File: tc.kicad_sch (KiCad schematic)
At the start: 6 parts

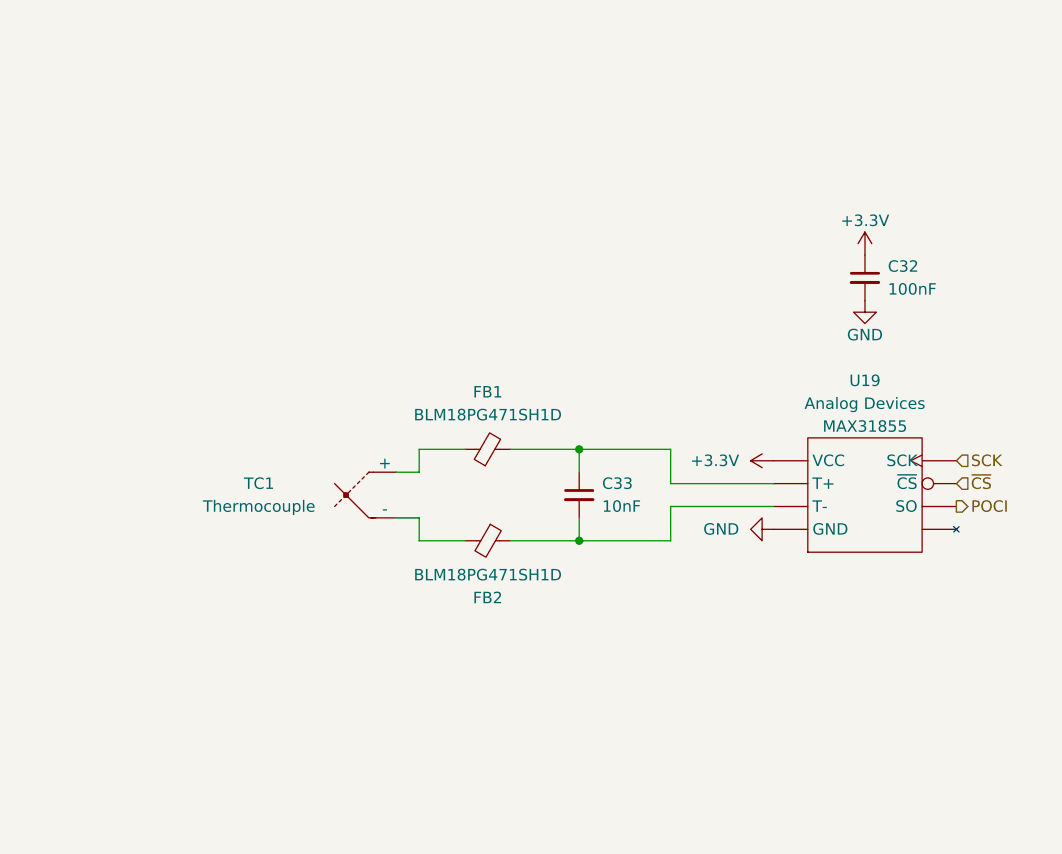
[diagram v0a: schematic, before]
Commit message: Updated schematic. No filtering but besides that finished. Need to fix footprints and start layout.
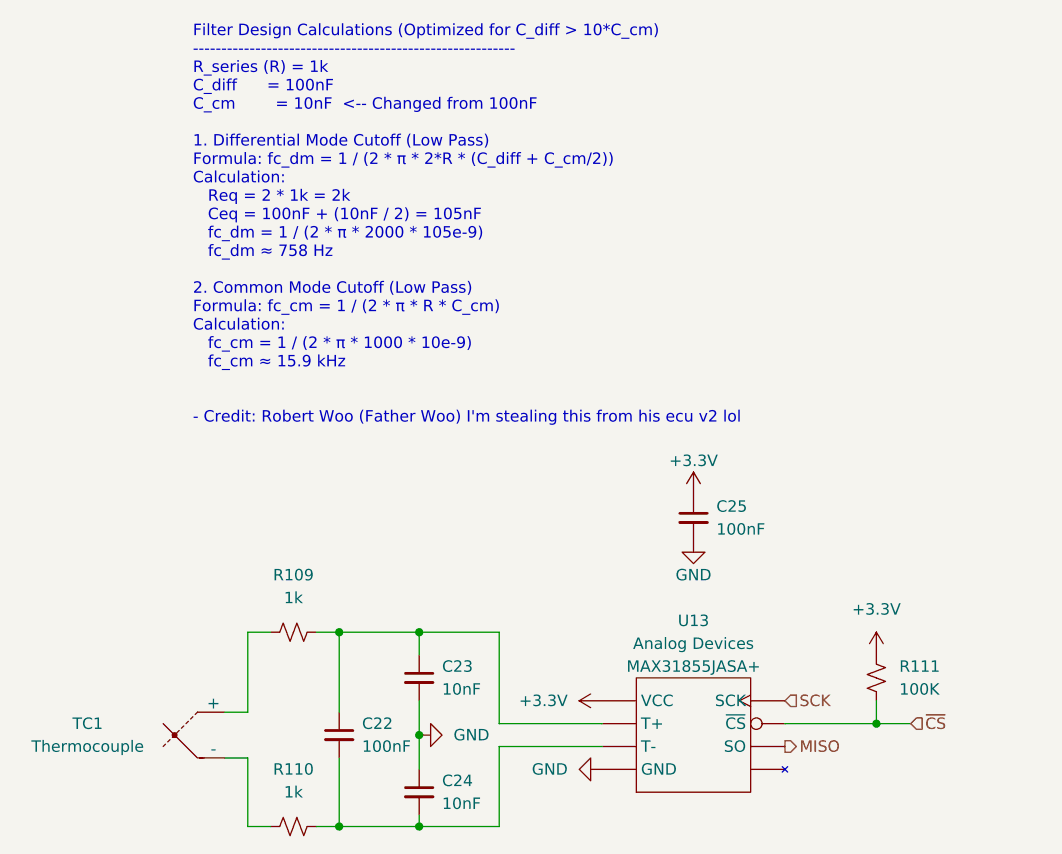
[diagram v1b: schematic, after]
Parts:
- removed C32: 100nF, Capacitor_SMD:C_0402_1005Metric, symbol Device:C_Small
- removed C33: 10nF, Capacitor_SMD:C_0402_1005Metric, symbol Device:C_Small
- removed FB1, FB2: BLM18PG471SH1D, Inductor_SMD:L_0603_1608Metric, symbol Device:FerriteBead_Small
- removed U19: ~, Package_SO:SOIC-8_3.9x4.9mm_P1.27mm, symbol UCIRP-KiCAD-Lib:MAX31855
- added C22, C25: 100nF, Capacitor_SMD:C_0402_1005Metric, symbol Device:C_Small
- added C23, C24: 10nF, Capacitor_SMD:C_0402_1005Metric, symbol Device:C_Small
- added R109, R110: 1k, Resistor_SMD:R_0402_1005Metric, symbol Device:R_Small_US
- added R111: 100K, Resistor_SMD:R_0402_1005Metric, symbol Device:R_Small_US
- added U13: ~, Package_SO:SOIC-8_3.9x4.9mm_P1.27mm, symbol UCIRP-KiCAD-Lib:MAX31855
- TC1: footprint UCIRP-KiCAD-Lib:AM-K-PCB -> 0UCIRP-KiCAD-Lib:AM-K-PCB
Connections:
- net +3.3V: now also C25.1, R111.1, U13.4 (VCC)
- net GND: now also C23.2, C24.1, C25.2, U13.1 (GND)
- net SCK: now also U13.5 (SCK)
- net ~{CS}: now also R111.2, U13.6 (~{CS})
- net at TC1.1 (+): now also R109.1
- net at TC1.2 (-): now also R110.1
- new net: C22.2, C24.2, R110.2, U13.2 (T-)
- new net: C22.1, C23.1, R109.2, U13.3 (T+)
- new net MISO: U13.7 (SO)
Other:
- note added: "Filter Design Calculations (Optimized for C_diff > 10*C_cm) --------------------------------------------------------- R_series (R) = 1k C_diff = 100nF C_cm = 10nF <-- Changed from 100nF 1. Differential Mode Cutoff (Low Pass) Formula: fc_dm = 1 / (2 * π * 2*R * (C_diff + C_cm/2)) Calculation: Req = 2 * 1k = 2k Ceq = 100nF + (10nF / 2) = 105nF fc_dm = 1 / (2 * π * 2000 * 105e-9) fc_dm ≈ 758 Hz 2. C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"

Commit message: Updates after PDR
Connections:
- net MISO renamed POCI
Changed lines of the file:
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@@
 		)
 	)
-	(hierarchical_label "MISO"
+	(hierarchical_label "POCI"
 		(shape output)
 		(at 160.02 125.73 0)

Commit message: Subsystem level layout done (prelim)
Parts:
- C22, C23, C24, C25: footprint Capacitor_SMD:C_0402_1005Metric -> Capacitor_SMD:C_0603_1608Metric
- R109, R110, R111: footprint Resistor_SMD:R_0402_1005Metric -> Resistor_SMD:R_0603_1608Metric
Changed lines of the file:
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@@
 			)
 		)
-		(property "Footprint" "Resistor_SMD:R_0402_1005Metric"
+		(property "Footprint" "Resistor_SMD:R_0603_1608Metric"
 			(at 170.18 118.11 0)
 			(effects
@@
 			)
 		)
-		(property "Footprint" "Capacitor_SMD:C_0402_1005Metric"
+		(property "Footprint" "Capacitor_SMD:C_0603_1608Metric"
 			(at 110.49 124.46 0)
 			(effects
@@
 			)
 		)
-		(property "Footprint" "Resistor_SMD:R_0402_1005Metric"
+		(property "Footprint" "Resistor_SMD:R_0603_1608Metric"
 			(at 105.41 113.03 0)
 			(effects
@@
 			)
 		)
-		(property "Footprint" "Capacitor_SMD:C_0402_1005Metric"
+		(property "Footprint" "Capacitor_SMD:C_0603_1608Metric"
 			(at 149.86 100.33 0)
 			(effects
@@
 			)
 		)
-		(property "Footprint" "Capacitor_SMD:C_0402_1005Metric"
+		(property "Footprint" "Capacitor_SMD:C_0603_1608Metric"
 			(at 119.38 118.11 0)
 			(effects
@@
 			)
 		)
-		(property "Footprint" "Capacitor_SMD:C_0402_1005Metric"
+		(property "Footprint" "Capacitor_SMD:C_0603_1608Metric"
 			(at 119.38 130.81 0)
 			(effects
@@
 			)
 		)
-		(property "Footprint" "Resistor_SMD:R_0402_1005Metric"
+		(property "Footprint" "Resistor_SMD:R_0603_1608Metric"
 			(at 105.41 134.62 0)
 			(effects

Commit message: GSE v2.1: Updates for DSUB connectors for schematic only done. Layout needs a ton of work
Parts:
- U18: renamed from U13; value ~ -> MAX31855JASA+
- renumbered C22 to C38, C23 to C39, C24 to C40, C25 to C41, R109 to R63, R110 to R64, R111 to R65
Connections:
- net POCI renamed MISO

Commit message: GSE v2.1 done, just waiting on prop rn to finalize their sensor list
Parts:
- removed TC1: Thermocouple, 0UCIRP-KiCAD-Lib:AM-K-PCB, symbol Device:Thermocouple
- removed U18: MAX31855JASA+, Package_SO:SOIC-8_3.9x4.9mm_P1.27mm, symbol UCIRP-KiCAD-Lib:MAX31855
- added TC1: AM-K-PCB, 0UCIRP-KiCAD-Lib:TC_Connector AM-K-PCB, symbol 0UCIRP-KiCAD-Lib:TC_Connector AM-K-PCB
- added U18: MAX31855JASA+, Package_SO:SOIC-8_3.9x4.9mm_P1.27mm, symbol 0UCIRP-KiCAD-Lib:TC_ADC MAX31855JASA+
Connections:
- net +3.3V: now also U18.4 (VCC)
- net GND: now also U18.1 (GND)
- net MISO: now also U18.7 (SO)
- net SCK: now also U18.5 (SCK)
- net ~{CS}: now also U18.6 (~{CS})
- net at R63.1: now also TC1.1 (+)
- net at R64.1: now also TC1.2 (-)
- net at C38.2, C40.2, R64.2: now also U18.2 (T-)
- net at C38.1, C39.1, R63.2: now also U18.3 (T+)

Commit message: GSE v2.1: Done, ready for JLCPCB
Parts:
- renumbered R63 to R66, R64 to R67, R65 to R68
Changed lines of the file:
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@@
 		(on_board yes)
 		(dnp no)
-		(property "Reference" "#PWR0272"
+		(property "Reference" "#PWR0177"
 			(at 170.18 119.38 0)
 			(effects
@@
 			(project "gse2-hardware"
 				(path "/1eb2a3ff-e0fd-4343-8dba-716780a4d459/1100e4d4-33fd-47fc-9f59-96795f9d855c"
-					(reference "#PWR0272")
-					(unit 1)
-				)
-				(path "/1eb2a3ff-e0fd-4343-8dba-716780a4d459/35c5bb72-f929-48f0-b004-62aa4fd1a0f8"
-					(reference "#PWR0284")
-					(unit 1)
-				)
-				(path "/1eb2a3ff-e0fd-4343-8dba-716780a4d459/f315ae7e-24bb-4336-b1c5-213291358db7"
-					(reference "#PWR0278")
+					(reference "#PWR0177")
+					(unit 1)
+				)
+				(path "/1eb2a3ff-e0fd-4343-8dba-716780a4d459/35c5bb72-f929-48f0-b004-62aa4fd1a0f8"
+					(reference "#PWR0189")
+					(unit 1)
+				)
+				(path "/1eb2a3ff-e0fd-4343-8dba-716780a4d459/f315ae7e-24bb-4336-b1c5-213291358db7"
+					(reference "#PWR0183")
 					(unit 1)
 				)
@@
 		(dnp no)
 		(fields_autoplaced yes)
-		(property "Reference" "#PWR0269"
+		(property "Reference" "#PWR0172"
 			(at 125.73 124.46 0)
 			(effects
@@
 			(project "gse2-hardware"
 				(path "/1eb2a3ff-e0fd-4343-8dba-716780a4d459/1100e4d4-33fd-47fc-9f59-96795f9d855c"
-					(reference "#PWR0269")
-					(unit 1)
-				)
-				(path "/1eb2a3ff-e0fd-4343-8dba-716780a4d459/35c5bb72-f929-48f0-b004-62aa4fd1a0f8"
-					(reference "#PWR0281")
-					(unit 1)
-				)
-				(path "/1eb2a3ff-e0fd-4343-8dba-716780a4d459/f315ae7e-24bb-4336-b1c5-213291358db7"
-					(reference "#PWR0275")
+					(reference "#PWR0172")
+					(unit 1)
+				)
+				(path "/1eb2a3ff-e0fd-4343-8dba-716780a4d459/35c5bb72-f929-48f0-b004-62aa4fd1a0f8"
+					(reference "#PWR0184")
+					(unit 1)
+				)
+				(path "/1eb2a3ff-e0fd-4343-8dba-716780a4d459/f315ae7e-24bb-4336-b1c5-213291358db7"
+					(reference "#PWR0178")
 					(unit 1)
 				)
@@
 		(on_board yes)
 		(dnp no)
-		(property "Reference" "R65"
+		(property "Reference" "R68"
 			(at 172.72 116.84 0)
 			(effects
@@
 			(project "gse2-hardware"
 				(path "/1eb2a3ff-e0fd-4343-8dba-716780a4d459/1100e4d4-33fd-47fc-9f59-96795f9d855c"
-					(reference "R65")
-					(unit 1)
-				)
-				(path "/1eb2a3ff-e0fd-4343-8dba-716780a4d459/35c5bb72-f929-48f0-b004-62aa4fd1a0f8"
+					(reference "R68")
+					(unit 1)
+				)
+				(path "/1eb2a3ff-e0fd-4343-8dba-716780a4d459/35c5bb72-f929-48f0-b004-62aa4fd1a0f8"
+					(reference "R74")
+					(unit 1)
+				)
+				(path "/1eb2a3ff-e0fd-4343-8dba-716780a4d459/f315ae7e-24bb-4336-b1c5-213291358db7"
 					(reference "R71")
-					(unit 1)
-				)
-				(path "/1eb2a3ff-e0fd-4343-8dba-716780a4d459/f315ae7e-24bb-4336-b1c5-213291358db7"
-					(reference "R68")
 					(unit 1)
 				)
@@
 		(dnp no)
 		(fields_autoplaced yes)
-		(property "Reference" "R63"
+		(property "Reference" "R66"
 			(at 105.41 106.68 90)
 			(effects
@@
 			(project "gse2-hardware"
 				(path "/1eb2a3ff-e0fd-4343-8dba-716780a4d459/1100e4d4-33fd-47fc-9f59-96795f9d855c"
-					(reference "R63")
-					(unit 1)
-				)
-				(path "/1eb2a3ff-e0fd-4343-8dba-716780a4d459/35c5bb72-f929-48f0-b004-62aa4fd1a0f8"
+					(reference "R66")
+					(unit 1)
+				)
+				(path "/1eb2a3ff-e0fd-4343-8dba-716780a4d459/35c5bb72-f929-48f0-b004-62aa4fd1a0f8"
+					(reference "R72")
+					(unit 1)
+				)
+				(path "/1eb2a3ff-e0fd-4343-8dba-716780a4d459/f315ae7e-24bb-4336-b1c5-213291358db7"
 					(reference "R69")
-					(unit 1)
-				)
-				(path "/1eb2a3ff-e0fd-4343-8dba-716780a4d459/f315ae7e-24bb-4336-b1c5-213291358db7"
-					(reference "R66")
 					(unit 1)
 				)
@@
 		(on_board yes)
 		(dnp no)
-		(property "Reference" "#PWR0273"
+		(property "Reference" "#PWR0176"
 			(at 149.86 109.22 0)
 			(effects
@@
 			(project "gse2-hardware"
 				(path "/1eb2a3ff-e0fd-4343-8dba-716780a4d459/1100e4d4-33fd-47fc-9f59-96795f9d855c"
-					(reference "#PWR0273")
-					(unit 1)
-				)
-				(path "/1eb2a3ff-e0fd-4343-8dba-716780a4d459/35c5bb72-f929-48f0-b004-62aa4fd1a0f8"
-					(reference "#PWR0285")
-					(unit 1)
-				)
-				(path "/1eb2a3ff-e0fd-4343-8dba-716780a4d459/f315ae7e-24bb-4336-b1c5-213291358db7"
-					(reference "#PWR0279")
+					(reference "#PWR0176")
+					(unit 1)
+				)
+				(path "/1eb2a3ff-e0fd-4343-8dba-716780a4d459/35c5bb72-f929-48f0-b004-62aa4fd1a0f8"
+					(reference "#PWR0188")
+					(unit 1)
+				)
+				(path "/1eb2a3ff-e0fd-4343-8dba-716780a4d459/f315ae7e-24bb-4336-b1c5-213291358db7"
+					(reference "#PWR0182")
 					(unit 1)
 				)
@@
 		(dnp no)
 		(fields_autoplaced yes)
-		(property "Reference" "R64"
+		(property "Reference" "R67"
 			(at 105.41 128.27 90)
 			(effects
@@
 			(project "gse2-hardware"
 				(path "/1eb2a3ff-e0fd-4343-8dba-716780a4d459/1100e4d4-33fd-47fc-9f59-96795f9d855c"
-					(reference "R64")
-					(unit 1)
-				)
-				(path "/1eb2a3ff-e0fd-4343-8dba-716780a4d459/35c5bb72-f929-48f0-b004-62aa4fd1a0f8"
+					(reference "R67")
+					(unit 1)
+				)
+				(path "/1eb2a3ff-e0fd-4343-8dba-716780a4d459/35c5bb72-f929-48f0-b004-62aa4fd1a0f8"
+					(reference "R73")
+					(unit 1)
+				)
+				(path "/1eb2a3ff-e0fd-4343-8dba-716780a4d459/f315ae7e-24bb-4336-b1c5-213291358db7"
 					(reference "R70")
-					(unit 1)
-				)
-				(path "/1eb2a3ff-e0fd-4343-8dba-716780a4d459/f315ae7e-24bb-4336-b1c5-213291358db7"
-					(reference "R67")
 					(unit 1)
 				)
@@
 		(dnp no)
 		(fields_autoplaced yes)
-		(property "Reference" "#PWR0270"
+		(property "Reference" "#PWR0173"
 			(at 143.51 120.65 0)
 			(effects
@@
 			(project "gse2-hardware"
 				(path "/1eb2a3ff-e0fd-4343-8dba-716780a4d459/1100e4d4-33fd-47fc-9f59-96795f9d855c"
-					(reference "#PWR0270")
-					(unit 1)
-				)
-				(path "/1eb2a3ff-e0fd-4343-8dba-716780a4d459/35c5bb72-f929-48f0-b004-62aa4fd1a0f8"
-					(reference "#PWR0282")
-					(unit 1)
-				)
-				(path "/1eb2a3ff-e0fd-4343-8dba-716780a4d459/f315ae7e-24bb-4336-b1c5-213291358db7"
-					(reference "#PWR0276")
+					(reference "#PWR0173")
+					(unit 1)
+				)
+				(path "/1eb2a3ff-e0fd-4343-8dba-716780a4d459/35c5bb72-f929-48f0-b004-62aa4fd1a0f8"
+					(reference "#PWR0185")
+					(unit 1)
+				)
+				(path "/1eb2a3ff-e0fd-4343-8dba-716780a4d459/f315ae7e-24bb-4336-b1c5-213291358db7"
+					(reference "#PWR0179")
 					(unit 1)
 				)
@@
 		(on_board yes)
 		(dnp no)
-		(property "Reference" "#PWR0274"
+		(property "Reference" "#PWR0175"
 			(at 149.86 101.6 0)
 			(effects
@@
 			(project "gse2-hardware"
 				(path "/1eb2a3ff-e0fd-4343-8dba-716780a4d459/1100e4d4-33fd-47fc-9f59-96795f9d855c"
-					(reference "#PWR0274")
-					(unit 1)
-				)
-				(path "/1eb2a3ff-e0fd-4343-8dba-716780a4d459/35c5bb72-f929-48f0-b004-62aa4fd1a0f8"
-					(reference "#PWR0286")
-					(unit 1)
-				)
-				(path "/1eb2a3ff-e0fd-4343-8dba-716780a4d459/f315ae7e-24bb-4336-b1c5-213291358db7"
-					(reference "#PWR0280")
+					(reference "#PWR0175")
+					(unit 1)
+				)
+				(path "/1eb2a3ff-e0fd-4343-8dba-716780a4d459/35c5bb72-f929-48f0-b004-62aa4fd1a0f8"
+					(reference "#PWR0187")
+					(unit 1)
+				)
+				(path "/1eb2a3ff-e0fd-4343-8dba-716780a4d459/f315ae7e-24bb-4336-b1c5-213291358db7"
+					(reference "#PWR0181")
 					(unit 1)
 				)
@@
 		(dnp no)
 		(fields_autoplaced yes)
-		(property "Reference" "#PWR0271"
+		(property "Reference" "#PWR0174"
 			(at 133.35 128.27 0)
 			(effects
@@
 			(project "gse2-hardware"
 				(path "/1eb2a3ff-e0fd-4343-8dba-716780a4d459/1100e4d4-33fd-47fc-9f59-96795f9d855c"
-					(reference "#PWR0271")
-					(unit 1)
-				)
-				(path "/1eb2a3ff-e0fd-4343-8dba-716780a4d459/35c5bb72-f929-48f0-b004-62aa4fd1a0f8"
-					(reference "#PWR0283")
-					(unit 1)
-				)
-				(path "/1eb2a3ff-e0fd-4343-8dba-716780a4d459/f315ae7e-24bb-4336-b1c5-213291358db7"
-					(reference "#PWR0277")
-					(unit 1)
-				)
+					(reference "#PWR0174")
+					(unit 1)
+				)
+				(path "/1eb2a3ff-e0fd-4343-8dba-716780a4d459/35c5bb72-f929-48f0-b004-62aa4fd1a0f8"
+					(reference "#PWR0186")
+					(unit 1)
+				)
+				(path "/1eb2a3ff-e0fd-4343-8dba-716780a4d459/f315ae7e-24bb-4336-b1c5-213291358db7"
+					(reference "#PWR0180")
+					(unit 1)
+				)
